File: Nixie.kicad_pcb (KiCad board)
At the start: 2 copper layers, 215.1 x 106.3 mm, 58 parts, among them J1 Led output, J2 Led Input, J3 Conn_01x03, Q1 Q_NMOS_GSD, U1 74LVC1G79, U2 HV5122, U3 HV5122

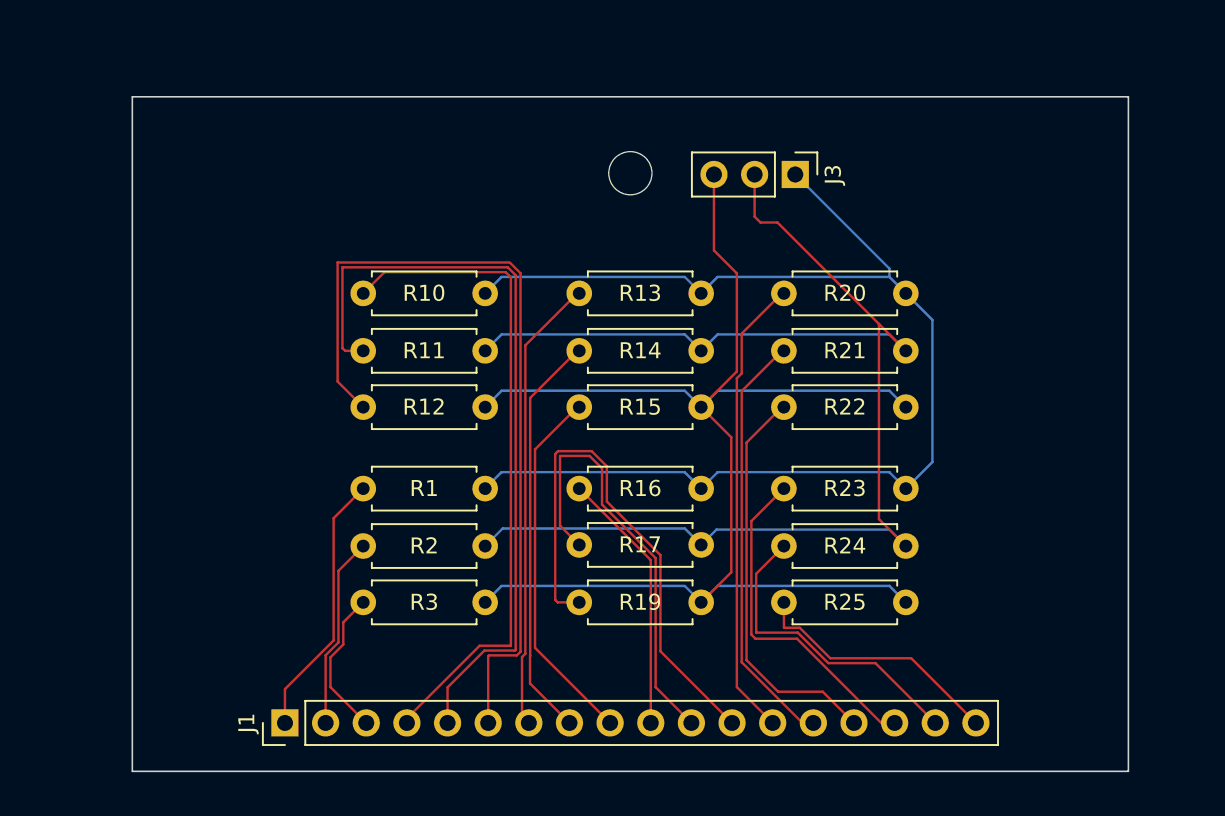
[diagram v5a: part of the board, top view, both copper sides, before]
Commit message: Update PCB mounting hole positions, layout routing, SVG export, and gerbers
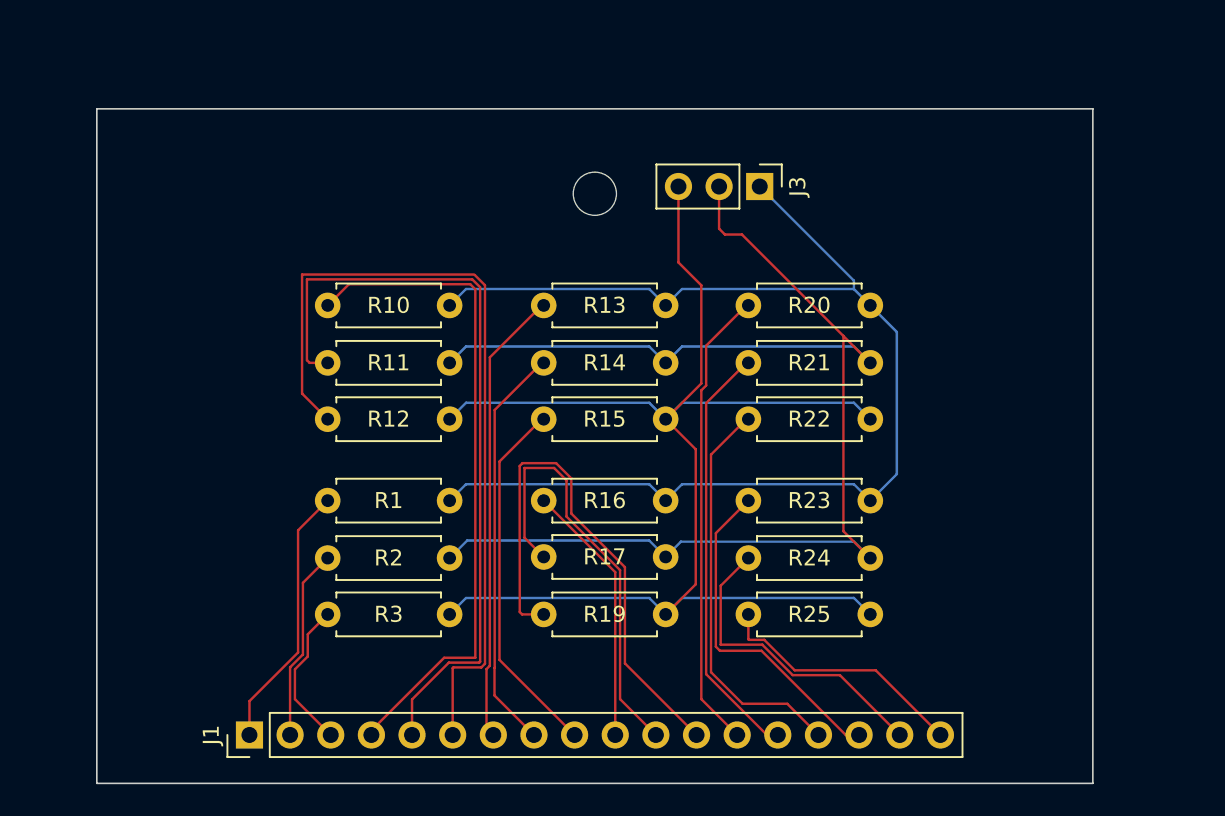
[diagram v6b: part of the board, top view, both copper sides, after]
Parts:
- moved REF** 2.56 mm to (152.1, 98.0)
- moved J1 2.34 mm to (130.5, 131.8)
- moved J3 2.34 mm to (162.4, 97.5)
- moved R1 2.34 mm to (135.4, 117.2)
- moved R10 2.34 mm to (135.4, 105.0)
- moved R11 2.34 mm to (135.4, 108.5)
- moved R12 2.34 mm to (135.4, 112.1)
- moved R13 2.34 mm to (148.9, 105.0)
- moved R14 2.34 mm to (148.9, 108.5)
- moved R15 2.34 mm to (148.9, 112.1)
- moved R16 2.34 mm to (148.9, 117.2)
- moved R17 2.34 mm to (148.9, 120.7)
- moved R19 2.34 mm to (148.9, 124.3)
- moved R2 2.34 mm to (135.4, 120.7)
- moved R20 2.34 mm to (161.7, 105.0)
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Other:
- board size 215.1 x 106.3 mm -> 215.1 x 107.1 mm

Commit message: Update design with PLCC-44 IC sockets and SK6812 MINI-E smart RGB LEDs
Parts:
- removed J1: Led output, Connector_PinHeader_2.54mm:PinHeader_1x18_P2.54mm_Vertical
- removed J2: Led Input, Connector_PinHeader_2.54mm:PinHeader_1x18_P2.54mm_Vertical
- removed J3: Conn_01x03, Connector_PinHeader_2.54mm:PinHeader_1x03_P2.54mm_Vertical
- removed R10, R13, R16, R20, R23: 100R, Resistor_THT:R_Axial_DIN0207_L6.3mm_D2.5mm_P7.62mm_Horizontal
- removed R11, R12, R14, R15, R17, R19, R2, R21, R22, R24, R25, R3: 120R, Resistor_THT:R_Axial_DIN0207_L6.3mm_D2.5mm_P7.62mm_Horizontal
- removed the REF** at (152.1, 98.0)
- D1, D2, D3, D4, D6, D7: value Led_RGB_CA -> SK6812MINI-E; footprint LED_SMD:LED_Cree-PLCC4_5x5mm_CW -> LED_SMD:LED_SK6812MINI-E_3.2x2.8mm_P1.5mm_ReverseMount; moved to B.Cu
- JP1: footprint Connector_PinHeader_2.54mm:PinHeader_1x07_P2.54mm_Vertical -> Connector_PinHeader_2.54mm:PinHeader_1x08_P2.54mm_Vertical
- R1: value 100R -> 330R
- U2, U3: footprint HV5122PG-G:QFP80P1390X1390X235-44N -> Package_LCC:PLCC-44_THT-Socket
- moved R1 107.3 mm to (55.7, 45.2), turned to 180 degrees
- moved U1 14.5 mm to (254.5, 59.0), turned to -90 degrees
- moved C7 10.9 mm to (256.7, 47.9)
- moved R27 10.9 mm to (254.7, 36.8)
- moved C9 10.9 mm to (253.5, 47.9)
- moved JP1 7.63 mm to (43.5, 61.1)
- moved C8 7.20 mm to (55.0, 57.1)
- moved D5 7.20 mm to (44.1, 37.7)
- moved R18 7.20 mm to (49.2, 40.6)
- moved REF** 7.20 mm to (40.8, 71.3)
- moved C6 7.20 mm to (51.6, 57.1)
- moved REF** 7.20 mm to (40.9, 30.2)
- moved U3 6.80 mm to (234.5, 45.8)
- moved U2 6.78 mm to (69.7, 58.5)
- moved R26 6.39 mm to (237.0, 35.1)
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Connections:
- D1 pad 1: +5V -> GND
- D1 pad 2: Net-(D1-RK) -> /LED_DIN
- D1 pad 3: Net-(D1-GK) -> +5V
- D1 pad 4: Net-(D1-BK) -> Net-(D1-DOUT)
- D2 pad 1: +5V -> GND
- D2 pad 2: Net-(D2-RK) -> Net-(D1-DOUT)
- D2 pad 3: Net-(D2-GK) -> +5V
- D2 pad 4: Net-(D2-BK) -> Net-(D2-DOUT)
- D3 pad 1: +5V -> GND
- D3 pad 2: Net-(D3-RK) -> Net-(D2-DOUT)
- D3 pad 3: Net-(D3-GK) -> +5V
- D3 pad 4: Net-(D3-BK) -> Net-(D3-DOUT)
- D4 pad 1: +5V -> GND
- D4 pad 2: Net-(D4-RK) -> Net-(D3-DOUT)
- D4 pad 3: Net-(D4-GK) -> +5V
- D4 pad 4: Net-(D4-BK) -> Net-(D4-DOUT)
- D6 pad 1: +5V -> GND
- D6 pad 2: Net-(D6-RK) -> Net-(D4-DOUT)
- D6 pad 3: Net-(D6-GK) -> +5V
- D6 pad 4: Net-(D6-BK) -> Net-(D6-DOUT)
- D7 pad 1: +5V -> GND
- D7 pad 2: Net-(D7-RK) -> Net-(D6-DOUT)
- D7 pad 3: Net-(D7-GK) -> +5V
- D7 pad 4: Net-(D7-BK) -> unconnected-(D7-DOUT-Pad4)
- R1 pad 1: Net-(J1-Pin_1) -> /LED_DIN
- R1 pad 2: /R -> Net-(JP1-Pin_8)
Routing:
- net /G: track 86.1 -> 0.00 mm
- net /B: track 85.8 -> 0.00 mm
- net /LED_DIN: track 0.00 -> 82.7 mm, vias 0 -> 3
- net /R: track 78.9 -> 0.00 mm
- net Net-(D7-BK): track 74.3 -> 0.00 mm
- net Net-(D1-BK): track 70.2 -> 0.00 mm
- net Net-(D7-GK): track 69.8 -> 0.00 mm
- net Net-(D1-GK): track 66.0 -> 0.00 mm
- net Net-(D7-RK): track 58.2 -> 0.00 mm
- net Net-(D1-RK): track 57.9 -> 0.00 mm
- net Net-(D2-BK): track 53.9 -> 0.00 mm
- net +5V: track 499.9 -> 446.9 mm, vias 13 -> 6
- net /40: track 70.6 -> 122.8 mm, vias 1 -> 0
- net Net-(J1-Pin_6): track 51.3 -> 0.00 mm
- net Net-(D2-GK): track 50.8 -> 0.00 mm
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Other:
- board size 215.1 x 107.1 mm -> 237 x 48.9 mm
